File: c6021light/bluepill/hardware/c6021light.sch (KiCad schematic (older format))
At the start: 69 parts, among them J1 Barrel_Jack_Switch, J10 Conn_01x02, J11 Conn_01x02, J12 XpressNet, J2 Conn_01x02, J3 Conn_02x16_Row_Letter_First, J30 Loconet, J4 Conn_01x02, J5 Grove I2C, J50 USB_B_Micro, J51 Conn_01x06, J52 Debug UART, J6 Conn_01x02, J7 Conn_01x02, J8 RJ45, Q30 BC337, U1 L7805, U10 SN75176, U2 L7808, U3 MCP2562, U30 LM393, U4 ISO1050DUB, U50 CH340C

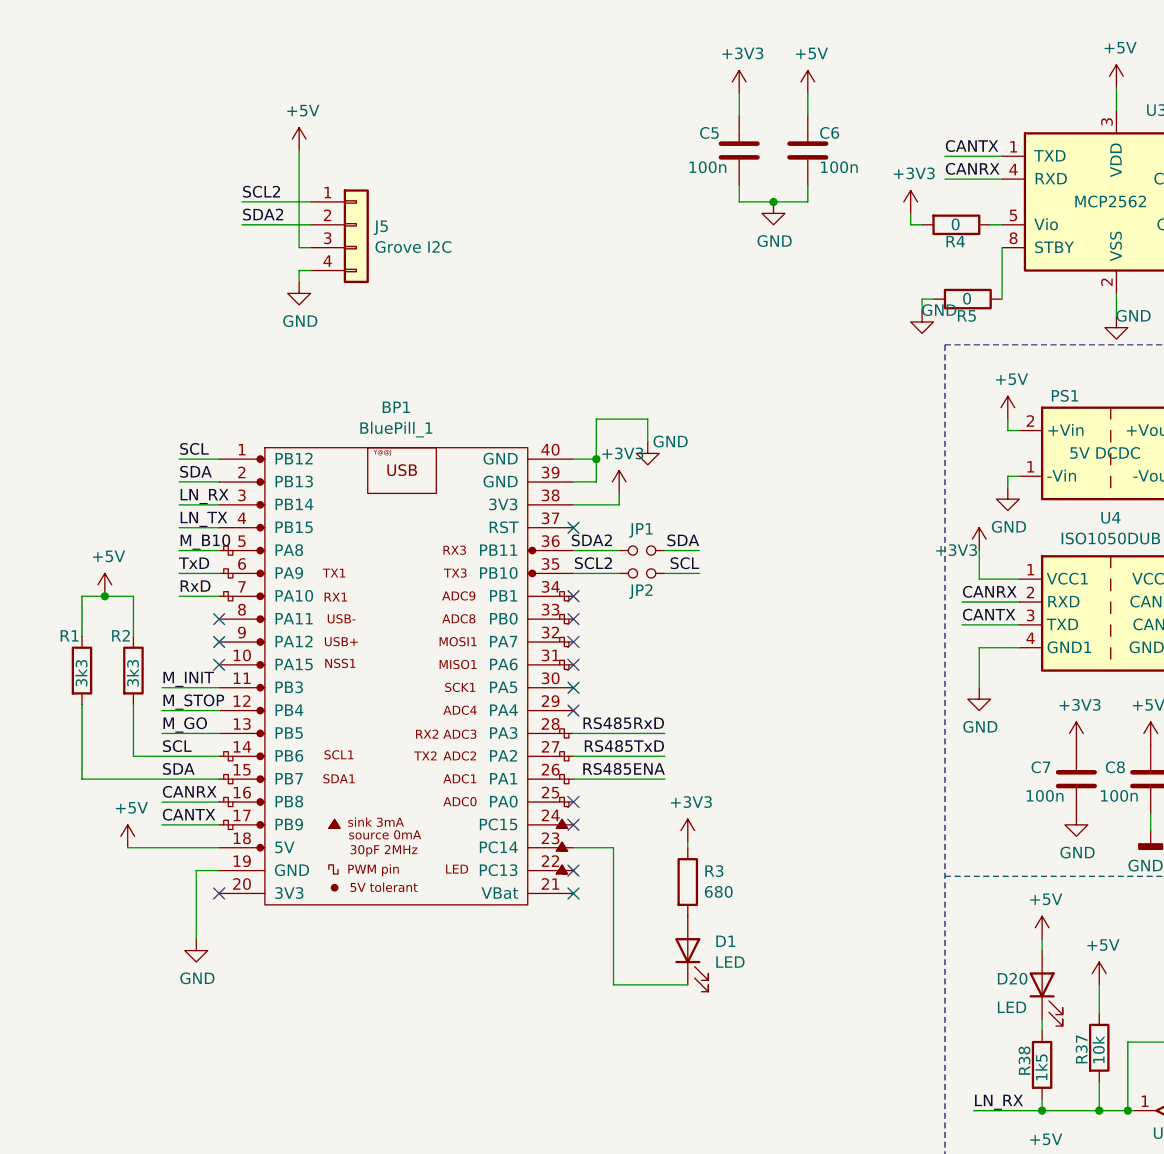
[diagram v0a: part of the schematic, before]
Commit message: fix PB2 (no 5V) and add push button
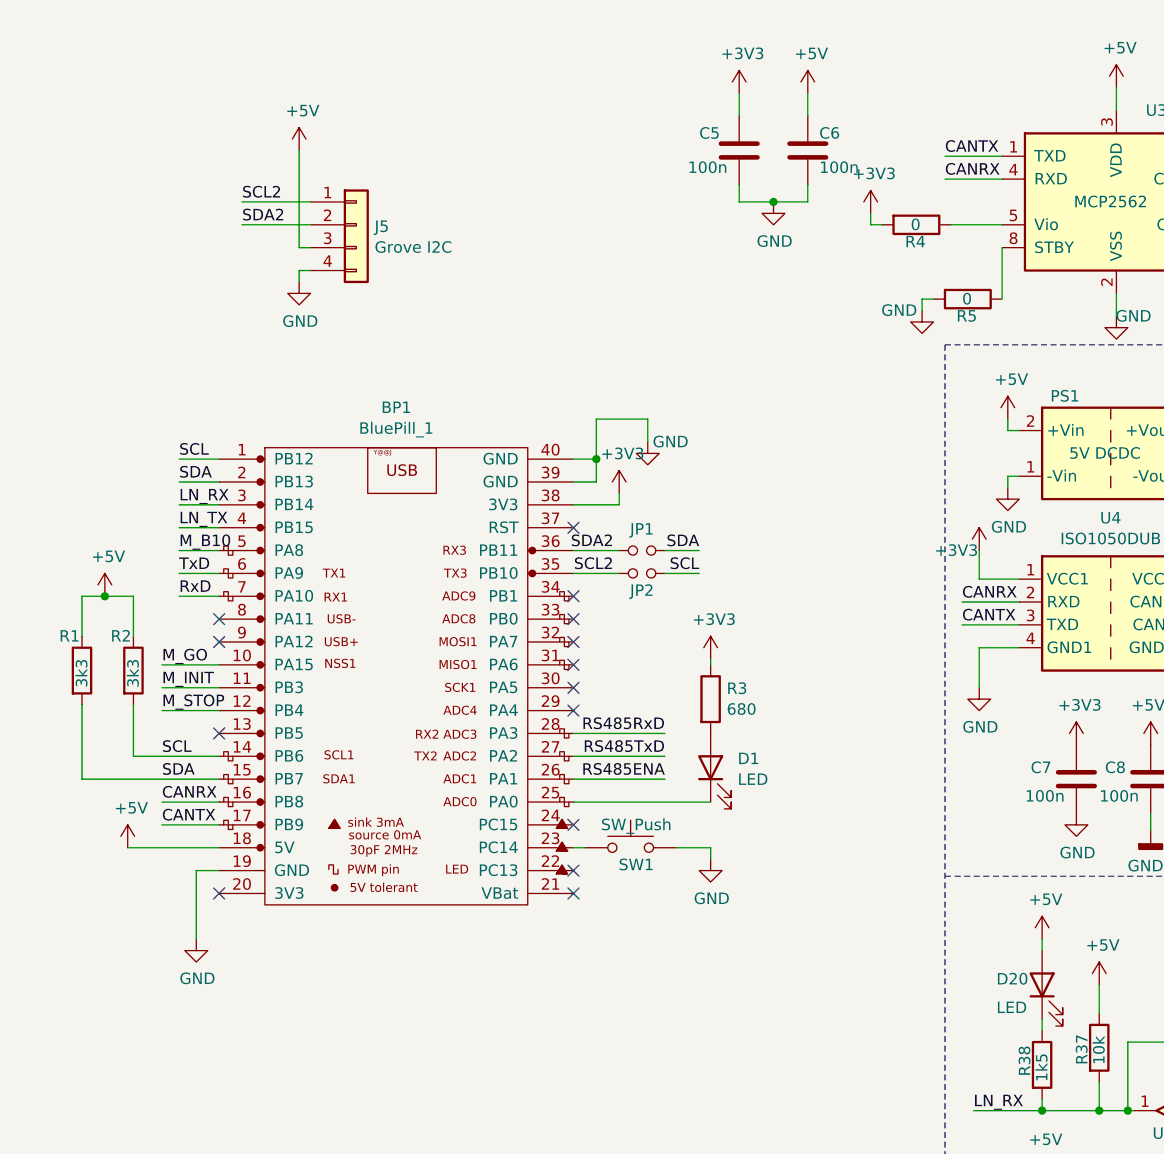
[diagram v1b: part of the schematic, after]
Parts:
- added SW1: SW_Push, symbol Switch:SW_Push
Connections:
- net GND: now also SW1.2
- net M_GO: now also BP1.10 (PA15); no longer BP1.13 (PB5)
- net at BP1.23 (PC14): now also SW1.1; no longer D1.1 (K)
- net at BP1.25 (PA0): now also D1.1 (K)
- no-connect marks 33 -> 32
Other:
- moved on the sheet: D1, R3, R4
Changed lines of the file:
@@
 NoConn ~ 5350 4425
 NoConn ~ 5350 4325
-NoConn ~ 5350 4125
-NoConn ~ 5350 4025
 NoConn ~ 5350 3125
 NoConn ~ 5350 3225
@@
 NoConn ~ 3800 3225
 NoConn ~ 3800 3325
-NoConn ~ 3800 3425
 Wire Wire Line
 	3800 4125 3550 4125
@@
 L power:+3V3 #PWR0108
 U 1 1 5ED9A0AB
-P 6825 1450
-F 0 "#PWR0108" H 6825 1300 50  0001 C CNN
-F 1 "+3V3" H 6840 1623 50  0000 C CNN
-F 2 "" H 6825 1450 50  0001 C CNN
-F 3 "" H 6825 1450 50  0001 C CNN
-	1    6825 1450
-	1    0    0    -1
-$EndComp
-Wire Wire Line
-	6825 1500 6825 1450
+P 6650 1450
+F 0 "#PWR0108" H 6650 1300 50  0001 C CNN
+F 1 "+3V3" H 6665 1623 50  0000 C CNN
+F 2 "" H 6650 1450 50  0001 C CNN
+F 3 "" H 6650 1450 50  0001 C CNN
+	1    6650 1450
+	1    0    0    -1
+$EndComp
+Wire Wire Line
+	6650 1500 6650 1450
 Wire Wire Line
 	7225 1200 6975 1200
@@
 L Device:LED D1
 U 1 1 5F293D84
-P 5850 4675
-F 0 "D1" V 5889 4557 50  0000 R CNN
-F 1 "LED" V 5798 4557 50  0000 R CNN
-F 2 "LED_THT:LED_D5.0mm" H 5850 4675 50  0001 C CNN
-F 3 "~" H 5850 4675 50  0001 C CNN
-	1    5850 4675
+P 5950 3875
+F 0 "D1" V 5989 3757 50  0000 R CNN
+F 1 "LED" V 5898 3757 50  0000 R CNN
+F 2 "LED_THT:LED_D5.0mm" H 5950 3875 50  0001 C CNN
+F 3 "~" H 5950 3875 50  0001 C CNN
+	1    5950 3875
 	0    -1   -1   0
 $EndComp
-$Comp
-L power:+3V3 #PWR0130
-U 1 1 5F296192
-P 5850 4200
-F 0 "#PWR0130" H 5850 4050 50  0001 C CNN
-F 1 "+3V3" H 5865 4373 50  0000 C CNN
-F 2 "" H 5850 4200 50  0001 C CNN
-F 3 "" H 5850 4200 50  0001 C CNN
-	1    5850 4200
-	1    0    0    -1
-$EndComp
-Wire Wire Line
-	5850 4200 5850 4225
-Wire Wire Line
-	5850 4825 5525 4825
-Wire Wire Line
-	5525 4825 5525 4225
-Wire Wire Line
-	5525 4225 5350 4225
+Wire Wire Line
+	5950 3400 5950 3425
 $Comp
 L Device:R R3
 U 1 1 5F2B5CB8
-P 5850 4375
-F 0 "R3" H 5920 4421 50  0000 L CNN
-F 1 "680" H 5920 4330 50  0000 L CNN
-F 2 "Resistor_THT:R_Axial_DIN0207_L6.3mm_D2.5mm_P7.62mm_Horizontal" V 5780 4375 50  0001 C CNN
-F 3 "~" H 5850 4375 50  0001 C CNN
-	1    5850 4375
+P 5950 3575
+F 0 "R3" H 6020 3621 50  0000 L CNN
+F 1 "680" H 6020 3530 50  0000 L CNN
+F 2 "Resistor_THT:R_Axial_DIN0207_L6.3mm_D2.5mm_P7.62mm_Horizontal" V 5880 3575 50  0001 C CNN
+F 3 "~" H 5950 3575 50  0001 C CNN
+	1    5950 3575
 	1    0    0    -1
 $EndComp
@@
 Wire Wire Line
 	3800 3625 3550 3625
-Wire Wire Line
-	3800 3725 3550 3725
 Text Label 3550 3525 0    50   ~ 0
 M_INIT
 Text Label 3550 3625 0    50   ~ 0
 M_STOP
-Text Label 3550 3725 0    50   ~ 0
+Text Label 3550 3425 0    50   ~ 0
 M_GO
 Text Label 2200 4150 2    50   ~ 0
@@
 L Device:R R4
 U 1 1 5EEBE05E
-P 7025 1500
-F 0 "R4" V 7100 1450 50  0000 L CNN
-F 1 "0" V 7025 1475 50  0000 L CNN
-F 2 "Resistor_THT:R_Axial_DIN0207_L6.3mm_D2.5mm_P7.62mm_Horizontal" V 6955 1500 50  0001 C CNN
-F 3 "~" H 7025 1500 50  0001 C CNN
-	1    7025 1500
+P 6850 1500
+F 0 "R4" V 6925 1450 50  0000 L CNN
+F 1 "0" V 6850 1475 50  0000 L CNN
+F 2 "Resistor_THT:R_Axial_DIN0207_L6.3mm_D2.5mm_P7.62mm_Horizontal" V 6780 1500 50  0001 C CNN
+F 3 "~" H 6850 1500 50  0001 C CNN
+	1    6850 1500
 	0    1    1    0
 $EndComp
 Wire Wire Line
-	6825 1500 6875 1500
-Wire Wire Line
-	7175 1500 7225 1500
+	6650 1500 6700 1500
 Wire Wire Line
 	7725 1800 7725 1900
@@
 P 6875 1875
 F 0 "#PWR0109" H 6875 1625 50  0001 C CNN
-F 1 "GND" H 6950 1875 50  0000 C CNN
+F 1 "GND" H 6775 1875 50  0000 C CNN
 F 2 "" H 6875 1875 50  0001 C CNN
 F 3 "" H 6875 1875 50  0001 C CNN
@@
 Text Label 2725 4350 2    50   ~ 0
 M_B10
+Wire Wire Line
+	3800 3425 3550 3425
+NoConn ~ 3800 3725
+$Comp
+L Switch:SW_Push SW1
+U 1 1 5F09E946
+P 5600 4225
+F 0 "SW1" H 5625 4150 50  0000 C CNN
+F 1 "SW_Push" H 5625 4325 50  0000 C CNN
+F 2 "" H 5600 4425 50  0001 C CNN
+F 3 "~" H 5600 4425 50  0001 C CNN
+	1    5600 4225
+	1    0    0    -1
+$EndComp
+$Comp
+L power:+3V3 #PWR0130
+U 1 1 5F296192
+P 5950 3400
+F 0 "#PWR0130" H 5950 3250 50  0001 C CNN
+F 1 "+3V3" H 5965 3573 50  0000 C CNN
+F 2 "" H 5950 3400 50  0001 C CNN
+F 3 "" H 5950 3400 50  0001 C CNN
+	1    5950 3400
+	1    0    0    -1
+$EndComp
+Wire Wire Line
+	5350 4025 5950 4025
+NoConn ~ 5350 4125
+Wire Wire Line
+	5350 4225 5400 4225
+Wire Wire Line
+	5800 4225 5950 4225
+Wire Wire Line
+	5950 4225 5950 4275
+$Comp
+L power:GND #PWR0160
+U 1 1 5EDECAE2
+P 5950 4275
+F 0 "#PWR0160" H 5950 4025 50  0001 C CNN
+F 1 "GND" H 5955 4102 50  0000 C CNN
+F 2 "" H 5950 4275 50  0001 C CNN
+F 3 "" H 5950 4275 50  0001 C CNN
+	1    5950 4275
+	1    0    0    -1
+$EndComp
+Wire Wire Line
+	7000 1500 7225 1500
 $EndSCHEMATC

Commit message: wip
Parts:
- removed J2: Conn_01x02, Connector_PinHeader_2.54mm:PinHeader_1x02_P2.54mm_Vertical, symbol Connector_Generic:Conn_01x02
- C51: footprint Capacitor_THT:C_Disc_D5.0mm_W2.5mm_P2.50mm -> Capacitor_SMD:C_0805_2012Metric
- D1, D20, D21: footprint LED_THT:LED_D5.0mm -> LED_THT:LED_D3.0mm
- J51: footprint Connector_PinSocket_2.54mm:PinSocket_1x06_P2.54mm_Vertical -> Connector_PinHeader_2.00mm:PinHeader_1x06_P2.00mm_Vertical
- J52: footprint Connector_PinSocket_2.54mm:PinSocket_1x06_P2.54mm_Vertical -> Connector_PinHeader_2.54mm:PinHeader_1x06_P2.54mm_Vertical
- JP1, JP2: footprint Connector_PinSocket_2.54mm:PinSocket_1x02_P2.54mm_Vertical -> Connector_PinHeader_2.54mm:PinHeader_1x02_P2.54mm_Vertical
- SW1: footprint (none) -> w_switch:PCB_PUSH
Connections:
- net +5V: now also C2.1, U1.3 (OUT)
- net +8V: now also J3.b1 (Pin_b1), J3.b3 (Pin_b3); no longer J3.b14 (Pin_b14), J3.b16 (Pin_b16)
- net M_GO: now also J3.b9 (Pin_b9); no longer J3.b8 (Pin_b8)
- net M_INIT: now also J3.b5 (Pin_b5); no longer J3.b12 (Pin_b12)
- net M_STOP: now also J3.b11 (Pin_b11); no longer J3.b6 (Pin_b6)
- net SCL: now also J3.b13 (Pin_b13); no longer J3.b4 (Pin_b4)
- net SDA: now also J3.b15 (Pin_b15); no longer J3.b2 (Pin_b2)
- net at J3.b10 (Pin_b10): no longer J4.1 (Pin_1)
- net at J3.b7 (Pin_b7): now also J4.1 (Pin_1)
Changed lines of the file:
@@
 	1850 2700 1850 2800
-$Comp
-L Connector_Generic:Conn_01x02 J2
-U 1 1 5ED7F86F
-P 2525 1625
-F 0 "J2" V 2443 1705 50  0000 L CNN
-F 1 "Conn_01x02" V 2488 1705 50  0001 L CNN
-F 2 "Connector_PinHeader_2.54mm:PinHeader_1x02_P2.54mm_Vertical" H 2525 1625 50  0001 C CNN
-F 3 "~" H 2525 1625 50  0001 C CNN
-	1    2525 1625
-	0    1    1    0
-$EndComp
-Wire Wire Line
-	2425 1425 2175 1425
 $Comp
 L power:GND #PWR0103
@@
 F 0 "D1" V 5989 3757 50  0000 R CNN
 F 1 "LED" V 5898 3757 50  0000 R CNN
-F 2 "LED_THT:LED_D5.0mm" H 5950 3875 50  0001 C CNN
+F 2 "LED_THT:LED_D3.0mm" H 5950 3875 50  0001 C CNN
 F 3 "~" H 5950 3875 50  0001 C CNN
 	1    5950 3875
@@
 Connection ~ 1225 3550
 Wire Wire Line
-	1425 3550 1225 3550
-Wire Wire Line
 	1225 3650 1225 3750
 Connection ~ 1225 3650
 Wire Wire Line
-	1425 3650 1225 3650
-Wire Wire Line
 	1225 3750 1225 3850
 Connection ~ 1225 3750
 Wire Wire Line
-	1425 3750 1225 3750
-Wire Wire Line
 	1225 3850 1225 3950
 Connection ~ 1225 3850
 Wire Wire Line
-	1425 3850 1225 3850
-Wire Wire Line
 	1225 3950 1225 4050
 Connection ~ 1225 3950
 Wire Wire Line
-	1425 3950 1225 3950
-Wire Wire Line
 	1225 4050 1225 4150
 Connection ~ 1225 4050
 Wire Wire Line
-	1425 4050 1225 4050
-Wire Wire Line
 	1225 4150 1225 4250
 Connection ~ 1225 4150
 Wire Wire Line
-	1425 4150 1225 4150
-Wire Wire Line
 	1225 4250 1225 4350
 Connection ~ 1225 4250
 Wire Wire Line
-	1425 4250 1225 4250
-Wire Wire Line
 	1225 4350 1225 4450
 Connection ~ 1225 4350
 Wire Wire Line
-	1425 4350 1225 4350
-Wire Wire Line
 	1225 4450 1225 4550
 Connection ~ 1225 4450
 Wire Wire Line
-	1425 4450 1225 4450
-Wire Wire Line
 	1225 4550 1225 4650
 Connection ~ 1225 4550
 Wire Wire Line
-	1425 4550 1225 4550
-Wire Wire Line
 	1225 4650 1225 4750
 Connection ~ 1225 4650
 Wire Wire Line
-	1425 4650 1225 4650
-Wire Wire Line
 	1225 4750 1225 4850
 Connection ~ 1225 4750
 Wire Wire Line
-	1425 4750 1225 4750
-Wire Wire Line
 	1225 4850 1225 4950
 Connection ~ 1225 4850
 Wire Wire Line
-	1425 4850 1225 4850
-Wire Wire Line
 	1225 4950 1225 5100
 Connection ~ 1225 4950
-Wire Wire Line
-	1425 4950 1225 4950
 $Comp
 L power:GND #PWR0117
@@
 Wire Wire Line
 	1225 3450 1225 3550
-Wire Wire Line
-	1425 3450 1225 3450
 $Comp
 L Device:C C4
@@
 F 0 "D20" V 7425 5025 50  0000 R CNN
 F 1 "LED" V 7300 5025 50  0000 R CNN
-F 2 "LED_THT:LED_D5.0mm" H 7400 4825 50  0001 C CNN
+F 2 "LED_THT:LED_D3.0mm" H 7400 4825 50  0001 C CNN
 F 3 "~" H 7400 4825 50  0001 C CNN
 	1    7400 4825
@@
 F 0 "D21" V 7450 6050 50  0000 R CNN
 F 1 "LED" V 7350 6050 50  0000 R CNN
-F 2 "LED_THT:LED_D5.0mm" H 7400 5850 50  0001 C CNN
+F 2 "LED_THT:LED_D3.0mm" H 7400 5850 50  0001 C CNN
 F 3 "~" H 7400 5850 50  0001 C CNN
 	1    7400 5850
@@
 F 0 "C51" H 4625 6100 50  0000 L CNN
 F 1 "100n" H 4575 5925 50  0000 L CNN
-F 2 "Capacitor_THT:C_Disc_D5.0mm_W2.5mm_P2.50mm" H 4763 5850 50  0001 C CNN
+F 2 "Capacitor_SMD:C_0805_2012Metric" H 4763 5850 50  0001 C CNN
 F 3 "~" H 4725 6000 50  0001 C CNN
 	1    4725 6000
@@
 F 0 "J51" H 6025 6325 50  0000 L CNN
 F 1 "Conn_01x06" H 6155 6701 50  0001 L CNN
-F 2 "Connector_PinSocket_2.54mm:PinSocket_1x06_P2.54mm_Vertical" H 6075 6800 50  0001 C CNN
+F 2 "Connector_PinHeader_2.00mm:PinHeader_1x06_P2.00mm_Vertical" H 6075 6800 50  0001 C CNN
 F 3 "~" H 6075 6800 50  0001 C CNN
 	1    6075 6800
@@
 F 0 "J52" H 6755 6467 50  0000 L CNN
 F 1 "Debug UART" H 6500 6075 50  0000 L CNN
-F 2 "Connector_PinSocket_2.54mm:PinSocket_1x06_P2.54mm_Vertical" H 6675 6475 50  0001 C CNN
+F 2 "Connector_PinHeader_2.54mm:PinHeader_1x06_P2.54mm_Vertical" H 6675 6475 50  0001 C CNN
 F 3 "~" H 6675 6475 50  0001 C CNN
 	1    6675 6475
@@
 F 0 "JP1" H 5650 3018 50  0000 C CNN
 F 1 "Jumper_NO_Small" H 5650 3019 50  0001 C CNN
-F 2 "Connector_PinSocket_2.54mm:PinSocket_1x02_P2.54mm_Vertical" H 5650 2925 50  0001 C CNN
+F 2 "Connector_PinHeader_2.54mm:PinHeader_1x02_P2.54mm_Vertical" H 5650 2925 50  0001 C CNN
 F 3 "~" H 5650 2925 50  0001 C CNN
 	1    5650 2925
@@
 F 0 "JP2" H 5650 2950 50  0000 C CNN
 F 1 "Jumper_NO_Small" H 5650 3119 50  0001 C CNN
-F 2 "Connector_PinSocket_2.54mm:PinSocket_1x02_P2.54mm_Vertical" H 5650 3025 50  0001 C CNN
+F 2 "Connector_PinHeader_2.54mm:PinHeader_1x02_P2.54mm_Vertical" H 5650 3025 50  0001 C CNN
 F 3 "~" H 5650 3025 50  0001 C CNN
 	1    5650 3025
@@
 $EndComp
 $Comp
-L Connector_Generic:Conn_02x16_Row_Letter_First J3
-U 1 1 5EE1C5CE
-P 1625 4150
-F 0 "J3" H 1675 4975 50  0000 C CNN
-F 1 "Conn_02x16_Row_Letter_First" H 1675 4976 50  0001 C CNN
-F 2 "Connector_DIN:DIN41612_B2_2x16_Female_Vertical_THT" H 1625 4150 50  0001 C CNN
-F 3 "~" H 1625 4150 50  0001 C CNN
-	1    1625 4150
-	1    0    0    -1
-$EndComp
-$Comp
 L Device:R R5
 U 1 1 5EE9C389
@@
 U 1 1 5F09E946
 P 5600 4225
-F 0 "SW1" H 5625 4150 50  0000 C CNN
-F 1 "SW_Push" H 5625 4325 50  0000 C CNN
-F 2 "" H 5600 4425 50  0001 C CNN
+F 0 "SW1" H 5600 4175 50  0000 C CNN
+F 1 "SW_Push" H 5625 4325 50  0001 C CNN
+F 2 "w_switch:PCB_PUSH" H 5600 4425 50  0001 C CNN
 F 3 "~" H 5600 4425 50  0001 C CNN
 	1    5600 4225
@@
 Wire Wire Line
 	7000 1500 7225 1500
+Wire Wire Line
+	1425 4250 1225 4250
+Wire Wire Line
+	1425 4150 1225 4150
+Wire Wire Line
+	1425 4050 1225 4050
+Wire Wire Line
+	1425 3950 1225 3950
+Wire Wire Line
+	1425 3850 1225 3850
+Wire Wire Line
+	1425 3750 1225 3750
+Wire Wire Line
+	1425 3650 1225 3650
+Wire Wire Line
+	1425 3550 1225 3550
+Wire Wire Line
+	1425 4950 1225 4950
+Wire Wire Line
+	1425 4850 1225 4850
+Wire Wire Line
+	1425 4750 1225 4750
+Wire Wire Line
+	1425 4650 1225 4650
+Wire Wire Line
+	1425 4550 1225 4550
+Wire Wire Line
+	1425 4450 1225 4450
+Wire Wire Line
+	1425 4350 1225 4350
+Wire Wire Line
+	1425 3450 1225 3450
+$Comp
+L Connector_Generic:Conn_02x16_Row_Letter_First J3
+U 1 1 5EE1C5CE
+P 1625 4250
+F 0 "J3" H 1675 5075 50  0000 C CNN
+F 1 "Conn_02x16_Row_Letter_First" H 1675 5076 50  0001 C CNN
+F 2 "Connector_DIN:DIN41612_B2_2x16_Female_Vertical_THT" H 1625 4250 50  0001 C CNN
+F 3 "~" H 1625 4250 50  0001 C CNN
+	1    1625 4250
+	1    0    0    1
+$EndComp
+Wire Wire Line
+	2175 1425 2525 1425
 $EndSCHEMATC
